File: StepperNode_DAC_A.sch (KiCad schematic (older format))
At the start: 9 parts, among them U26 AMC7812BSPAP

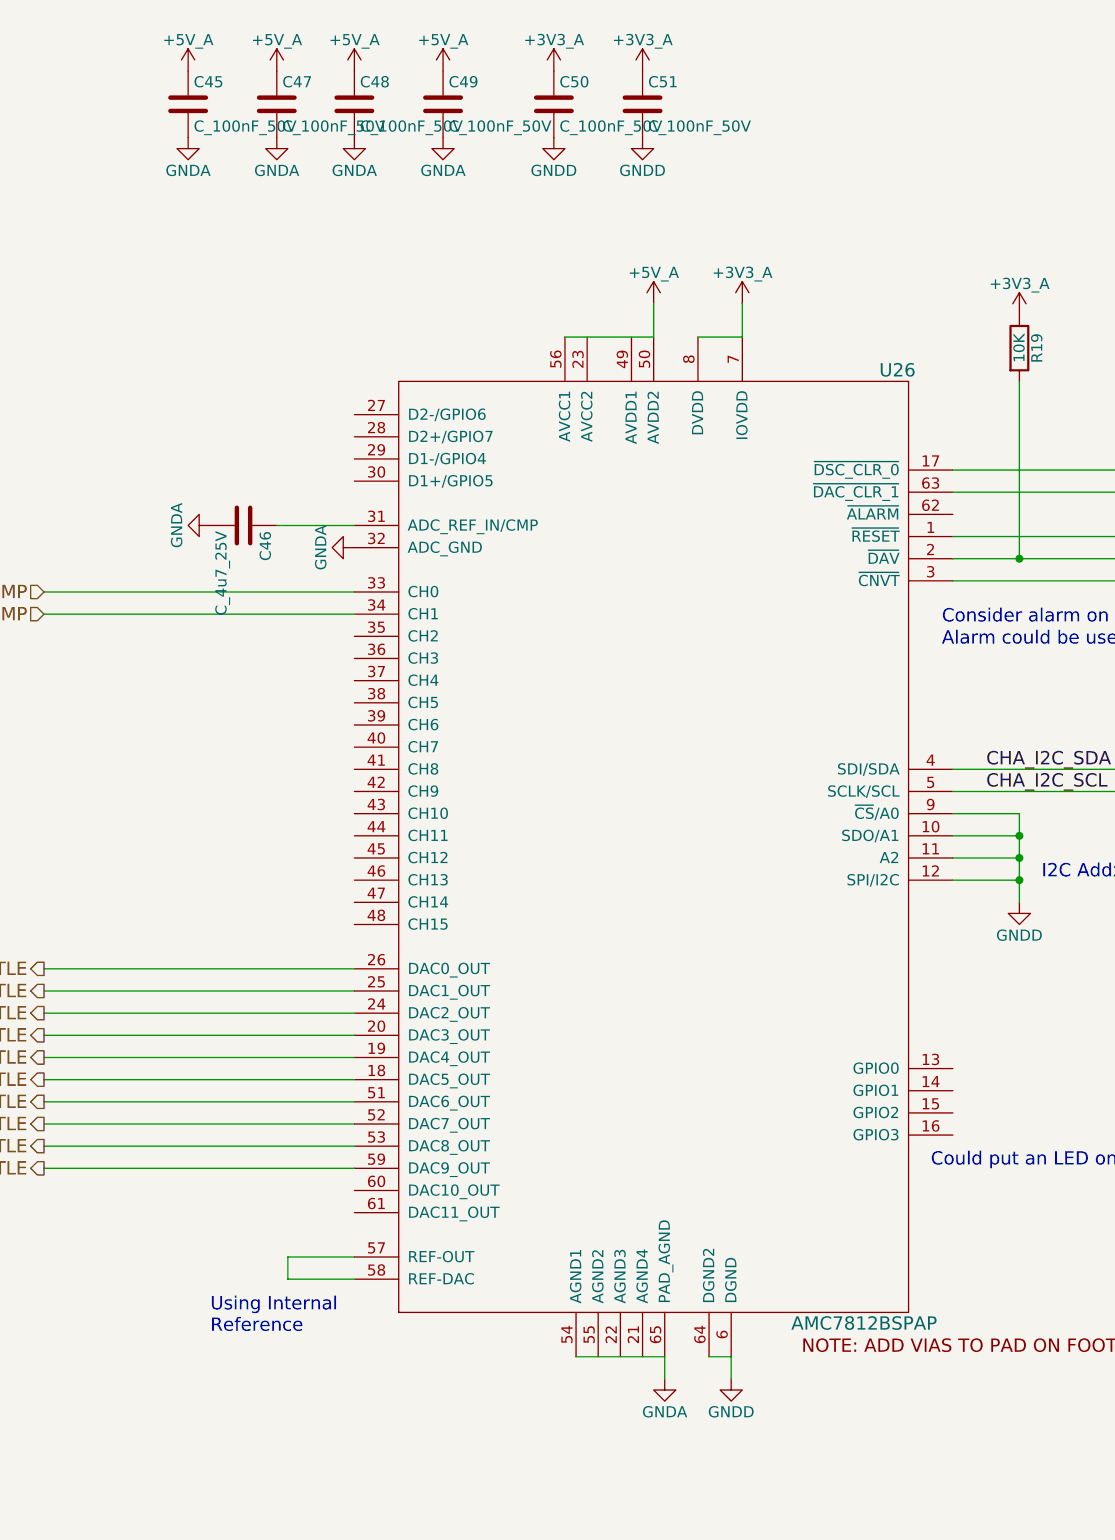
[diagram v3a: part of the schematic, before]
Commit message: Fix most ERC warnings (non-connected pins, etc)
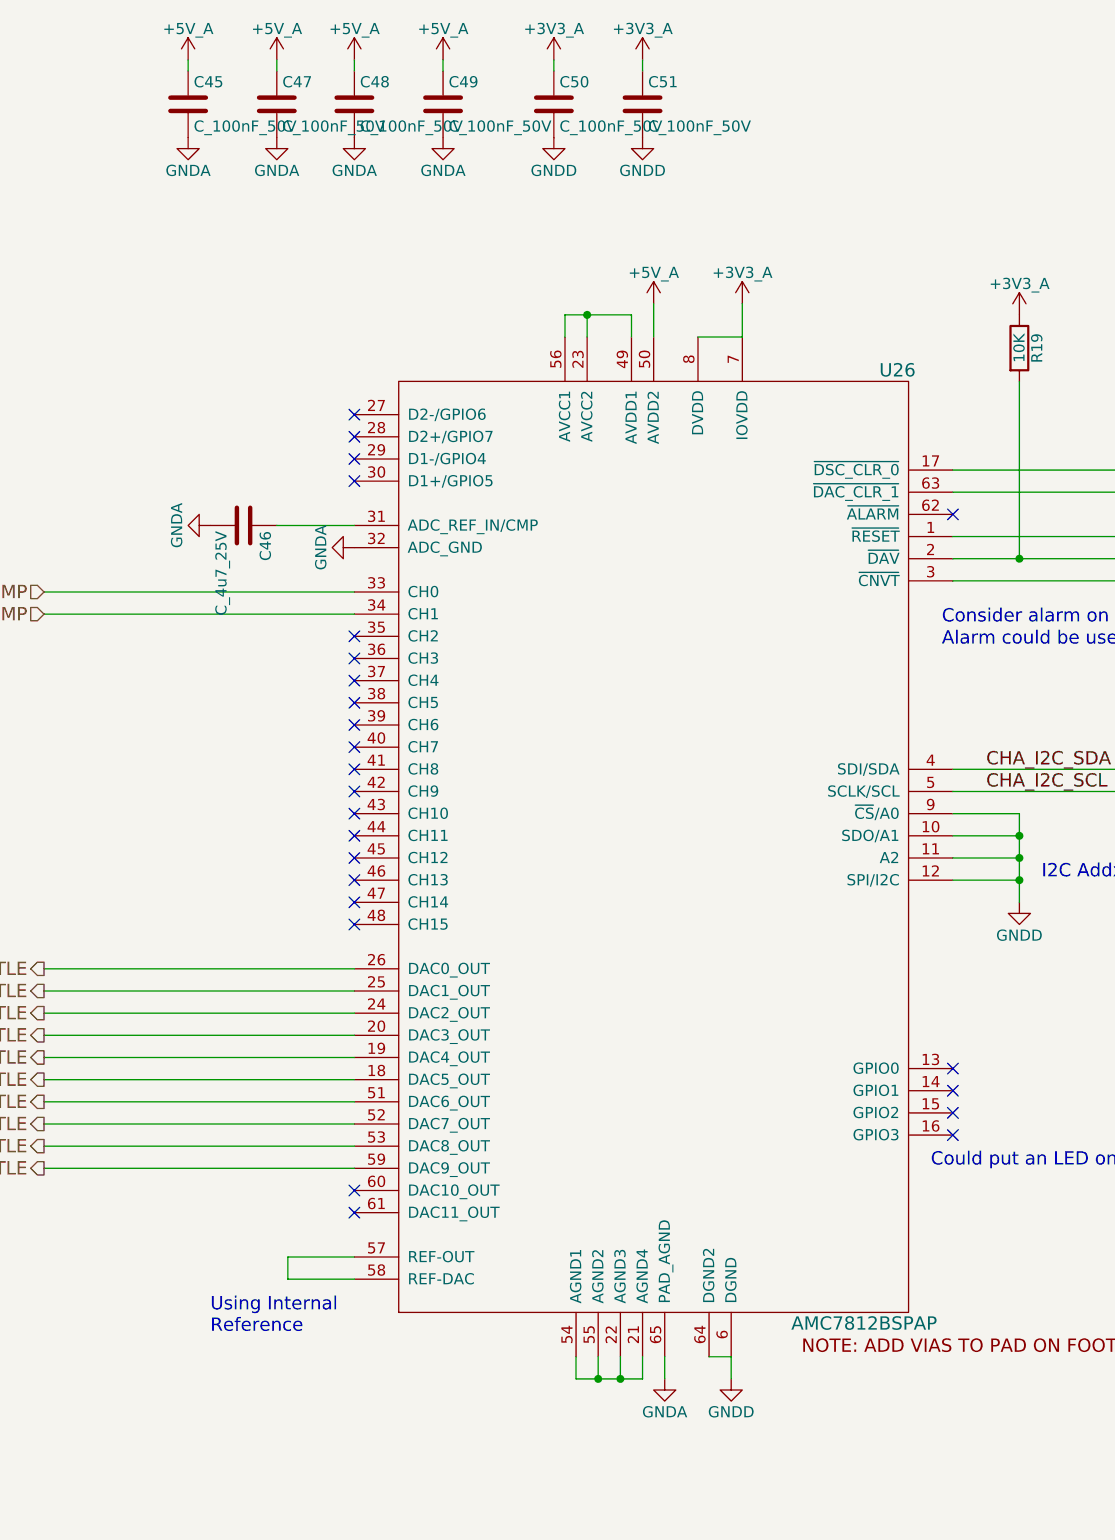
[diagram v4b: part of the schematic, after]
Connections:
- net +5V: no longer U26.56 (AVCC1)
- net GNDA: no longer U26.54 (AGND1)
- net at U26.21 (AGND4): now also U26.22 (AGND3), U26.54 (AGND1), U26.55 (AGND2)
- net at U26.23 (AVCC2): now also U26.49 (AVDD1), U26.56 (AVCC1)
- no-connect marks 0 -> 25
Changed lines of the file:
@@
 CHA_I2C_SCL
 $Comp
-L GNDD #PWR202
+L GNDD #PWR0194
 U 1 1 57505B54
 P 9450 4950
-F 0 "#PWR202" H 9450 4700 50  0001 C CNN
+F 0 "#PWR0194" H 9450 4700 50  0001 C CNN
 F 1 "GNDD" H 9450 4800 50  0000 C CNN
 F 2 "" H 9450 4950 50  0000 C CNN
@@
 I2C Addx = 0xC2,0xC3
 $Comp
-L GNDD #PWR199
+L GNDD #PWR0195
 U 1 1 57563E31
 P 8150 7100
-F 0 "#PWR199" H 8150 6850 50  0001 C CNN
+F 0 "#PWR0195" H 8150 6850 50  0001 C CNN
 F 1 "GNDD" H 8150 6950 50  0000 C CNN
 F 2 "" H 8150 7100 50  0000 C CNN
@@
 	6100 3250 6450 3250
 $Comp
-L GNDA #PWR198
+L GNDA #PWR0196
 U 1 1 57564064
 P 7850 7100
-F 0 "#PWR198" H 7850 6850 50  0001 C CNN
+F 0 "#PWR0196" H 7850 6850 50  0001 C CNN
 F 1 "GNDA" H 7850 6950 50  0000 C CNN
 F 2 "" H 7850 7100 50  0000 C CNN
@@
 $EndComp
 $Comp
-L GNDA #PWR190
+L GNDA #PWR0197
 U 1 1 5756407C
 P 6450 3350
-F 0 "#PWR190" H 6450 3100 50  0001 C CNN
+F 0 "#PWR0197" H 6450 3100 50  0001 C CNN
 F 1 "GNDA" H 6450 3200 50  0000 C CNN
 F 2 "" H 6450 3350 50  0000 C CNN
@@
 $EndComp
 Wire Wire Line
-	7450 7000 7850 7000
-Wire Wire Line
 	7850 7000 7850 7100
 Wire Wire Line
 	7800 2250 7800 2400
 Wire Wire Line
-	7800 2400 7400 2400
-Wire Wire Line
 	8200 2250 8200 2400
 Wire Wire Line
 	8200 2400 8000 2400
 $Comp
-L GNDA #PWR185
+L GNDA #PWR0198
 U 1 1 57564570
 P 5800 3250
-F 0 "#PWR185" H 5800 3000 50  0001 C CNN
+F 0 "#PWR0198" H 5800 3000 50  0001 C CNN
 F 1 "GNDA" H 5800 3100 50  0000 C CNN
 F 2 "" H 5800 3250 50  0000 C CNN
@@
 Wire Wire Line
 	6150 6650 6150 6550
-Wire Wire Line
-	6150 6550 6450 6550
 Text Notes 5800 6900 0    60   ~ 0
 Using Internal\nReference
@@
 Could put an LED on this for debug
 $Comp
-L GNDA #PWR184
+L GNDA #PWR0199
 U 1 1 57564AC5
 P 5700 1500
-F 0 "#PWR184" H 5700 1250 50  0001 C CNN
+F 0 "#PWR0199" H 5700 1250 50  0001 C CNN
 F 1 "GNDA" H 5700 1350 50  0000 C CNN
 F 2 "" H 5700 1500 50  0000 C CNN
@@
 $EndComp
 $Comp
-L GNDA #PWR187
+L GNDA #PWR0200
 U 1 1 57564BE5
 P 6100 1500
-F 0 "#PWR187" H 6100 1250 50  0001 C CNN
+F 0 "#PWR0200" H 6100 1250 50  0001 C CNN
 F 1 "GNDA" H 6100 1350 50  0000 C CNN
 F 2 "" H 6100 1500 50  0000 C CNN
@@
 $EndComp
 $Comp
-L GNDA #PWR189
+L GNDA #PWR0201
 U 1 1 57564C44
 P 6450 1500
-F 0 "#PWR189" H 6450 1250 50  0001 C CNN
+F 0 "#PWR0201" H 6450 1250 50  0001 C CNN
 F 1 "GNDA" H 6450 1350 50  0000 C CNN
 F 2 "" H 6450 1500 50  0000 C CNN
@@
 $EndComp
 $Comp
-L GNDA #PWR192
+L GNDA #PWR0202
 U 1 1 57564C56
 P 6850 1500
-F 0 "#PWR192" H 6850 1250 50  0001 C CNN
+F 0 "#PWR0202" H 6850 1250 50  0001 C CNN
 F 1 "GNDA" H 6850 1350 50  0000 C CNN
 F 2 "" H 6850 1500 50  0000 C CNN
@@
 $EndComp
 $Comp
-L GNDD #PWR194
+L GNDD #PWR0203
 U 1 1 57564D4D
 P 7350 1500
-F 0 "#PWR194" H 7350 1250 50  0001 C CNN
+F 0 "#PWR0203" H 7350 1250 50  0001 C CNN
 F 1 "GNDD" H 7350 1350 50  0000 C CNN
 F 2 "" H 7350 1500 50  0000 C CNN
@@
 $EndComp
 $Comp
-L GNDD #PWR196
+L GNDD #PWR0204
 U 1 1 57564D89
 P 7750 1500
-F 0 "#PWR196" H 7750 1250 50  0001 C CNN
+F 0 "#PWR0204" H 7750 1250 50  0001 C CNN
 F 1 "GNDD" H 7750 1350 50  0000 C CNN
 F 2 "" H 7750 1500 50  0000 C CNN
@@
 $EndComp
 $Comp
-L +3V3_A #PWR201
+L +3V3_A #PWR0205
 U 1 1 5766CA48
 P 9450 2300
-F 0 "#PWR201" H 9450 2150 50  0001 C CNN
+F 0 "#PWR0205" H 9450 2150 50  0001 C CNN
 F 1 "+3V3_A" H 9450 2440 50  0000 C CNN
 F 2 "" H 9450 2300 60  0000 C CNN
@@
 $EndComp
 $Comp
-L +3V3_A #PWR200
+L +3V3_A #PWR0206
 U 1 1 5766CA6C
 P 8200 2250
-F 0 "#PWR200" H 8200 2100 50  0001 C CNN
+F 0 "#PWR0206" H 8200 2100 50  0001 C CNN
 F 1 "+3V3_A" H 8200 2390 50  0000 C CNN
 F 2 "" H 8200 2250 60  0000 C CNN
@@
 $EndComp
 $Comp
-L +3V3_A #PWR195
+L +3V3_A #PWR0207
 U 1 1 5766CB47
-P 7750 1200
-F 0 "#PWR195" H 7750 1050 50  0001 C CNN
-F 1 "+3V3_A" H 7750 1340 50  0000 C CNN
-F 2 "" H 7750 1200 60  0000 C CNN
-F 3 "" H 7750 1200 60  0000 C CNN
-	1    7750 1200
-	1    0    0    -1
-$EndComp
-$Comp
-L +3V3_A #PWR193
+P 7750 1150
+F 0 "#PWR0207" H 7750 1000 50  0001 C CNN
+F 1 "+3V3_A" H 7750 1290 50  0000 C CNN
+F 2 "" H 7750 1150 60  0000 C CNN
+F 3 "" H 7750 1150 60  0000 C CNN
+	1    7750 1150
+	1    0    0    -1
+$EndComp
+$Comp
+L +3V3_A #PWR0208
 U 1 1 5766CB58
-P 7350 1200
-F 0 "#PWR193" H 7350 1050 50  0001 C CNN
-F 1 "+3V3_A" H 7350 1340 50  0000 C CNN
-F 2 "" H 7350 1200 60  0000 C CNN
-F 3 "" H 7350 1200 60  0000 C CNN
-	1    7350 1200
-	1    0    0    -1
-$EndComp
-$Comp
-L +5V_A #PWR191
+P 7350 1150
+F 0 "#PWR0208" H 7350 1000 50  0001 C CNN
+F 1 "+3V3_A" H 7350 1290 50  0000 C CNN
+F 2 "" H 7350 1150 60  0000 C CNN
+F 3 "" H 7350 1150 60  0000 C CNN
+	1    7350 1150
+	1    0    0    -1
+$EndComp
+$Comp
+L +5V_A #PWR0209
 U 1 1 5766CCBC
-P 6850 1200
-F 0 "#PWR191" H 6850 1050 50  0001 C CNN
-F 1 "+5V_A" H 6850 1340 50  0000 C CNN
-F 2 "" H 6850 1200 60  0000 C CNN
-F 3 "" H 6850 1200 60  0000 C CNN
-	1    6850 1200
-	1    0    0    -1
-$EndComp
-$Comp
-L +5V_A #PWR188
+P 6850 1150
+F 0 "#PWR0209" H 6850 1000 50  0001 C CNN
+F 1 "+5V_A" H 6850 1290 50  0000 C CNN
+F 2 "" H 6850 1150 60  0000 C CNN
+F 3 "" H 6850 1150 60  0000 C CNN
+	1    6850 1150
+	1    0    0    -1
+$EndComp
+$Comp
+L +5V_A #PWR0210
 U 1 1 5766CCE0
-P 6450 1200
-F 0 "#PWR188" H 6450 1050 50  0001 C CNN
-F 1 "+5V_A" H 6450 1340 50  0000 C CNN
-F 2 "" H 6450 1200 60  0000 C CNN
-F 3 "" H 6450 1200 60  0000 C CNN
-	1    6450 1200
-	1    0    0    -1
-$EndComp
-$Comp
-L +5V_A #PWR186
+P 6450 1150
+F 0 "#PWR0210" H 6450 1000 50  0001 C CNN
+F 1 "+5V_A" H 6450 1290 50  0000 C CNN
+F 2 "" H 6450 1150 60  0000 C CNN
+F 3 "" H 6450 1150 60  0000 C CNN
+	1    6450 1150
+	1    0    0    -1
+$EndComp
+$Comp
+L +5V_A #PWR0211
 U 1 1 5766CCF1
-P 6100 1200
-F 0 "#PWR186" H 6100 1050 50  0001 C CNN
-F 1 "+5V_A" H 6100 1340 50  0000 C CNN
-F 2 "" H 6100 1200 60  0000 C CNN
-F 3 "" H 6100 1200 60  0000 C CNN
-	1    6100 1200
-	1    0    0    -1
-$EndComp
-$Comp
-L +5V_A #PWR183
+P 6100 1150
+F 0 "#PWR0211" H 6100 1000 50  0001 C CNN
+F 1 "+5V_A" H 6100 1290 50  0000 C CNN
+F 2 "" H 6100 1150 60  0000 C CNN
+F 3 "" H 6100 1150 60  0000 C CNN
+	1    6100 1150
+	1    0    0    -1
+$EndComp
+$Comp
+L +5V_A #PWR0212
 U 1 1 5766CD02
-P 5700 1200
-F 0 "#PWR183" H 5700 1050 50  0001 C CNN
-F 1 "+5V_A" H 5700 1340 50  0000 C CNN
-F 2 "" H 5700 1200 60  0000 C CNN
-F 3 "" H 5700 1200 60  0000 C CNN
-	1    5700 1200
-	1    0    0    -1
-$EndComp
-$Comp
-L +5V_A #PWR197
+P 5700 1150
+F 0 "#PWR0212" H 5700 1000 50  0001 C CNN
+F 1 "+5V_A" H 5700 1290 50  0000 C CNN
+F 2 "" H 5700 1150 60  0000 C CNN
+F 3 "" H 5700 1150 60  0000 C CNN
+	1    5700 1150
+	1    0    0    -1
+$EndComp
+$Comp
+L +5V_A #PWR0213
 U 1 1 5766CD13
 P 7800 2250
-F 0 "#PWR197" H 7800 2100 50  0001 C CNN
+F 0 "#PWR0213" H 7800 2100 50  0001 C CNN
 F 1 "+5V_A" H 7800 2390 50  0000 C CNN
 F 2 "" H 7800 2250 60  0000 C CNN
@@
 	0    1    1    0
 $EndComp
+NoConn ~ 6450 3750
+NoConn ~ 6450 3850
+NoConn ~ 6450 3950
+NoConn ~ 6450 4050
+NoConn ~ 6450 4150
+NoConn ~ 6450 4250
+NoConn ~ 6450 4450
+NoConn ~ 6450 4550
+NoConn ~ 6450 4650
+NoConn ~ 6450 4750
+NoConn ~ 6450 4850
+NoConn ~ 6450 4950
+NoConn ~ 6450 5050
+NoConn ~ 6450 6250
+NoConn ~ 6450 6350
+NoConn ~ 6450 4350
+NoConn ~ 9150 3200
+NoConn ~ 9150 5700
+NoConn ~ 9150 5800
+NoConn ~ 9150 5900
+NoConn ~ 9150 6000
+Wire Wire Line
+	7450 7000 7450 7100
+Wire Wire Line
+	7450 7100 7750 7100
+Wire Wire Line
+	7750 7100 7750 7000
+Wire Wire Line
+	7550 7000 7550 7100
+Connection ~ 7550 7100
+Wire Wire Line
+	7650 7000 7650 7100
+Connection ~ 7650 7100
+Wire Wire Line
+	6150 6550 6450 6550
+NoConn ~ 6450 2750
+NoConn ~ 6450 2850
+NoConn ~ 6450 2950
+NoConn ~ 6450 3050
+Wire Wire Line
+	7400 2400 7400 2300
+Wire Wire Line
+	7400 2300 7700 2300
+Wire Wire Line
+	7700 2300 7700 2400
+Wire Wire Line
+	7500 2400 7500 2300
+Connection ~ 7500 2300
+Wire Wire Line
+	6100 1200 6100 1150
+Wire Wire Line
+	5700 1150 5700 1200
+Wire Wire Line
+	6450 1150 6450 1200
+Wire Wire Line
+	6850 1150 6850 1200
+Wire Wire Line
+	7350 1150 7350 1200
+Wire Wire Line
+	7750 1150 7750 1200
 $EndSCHEMATC
